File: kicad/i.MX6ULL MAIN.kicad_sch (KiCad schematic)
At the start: 3 parts

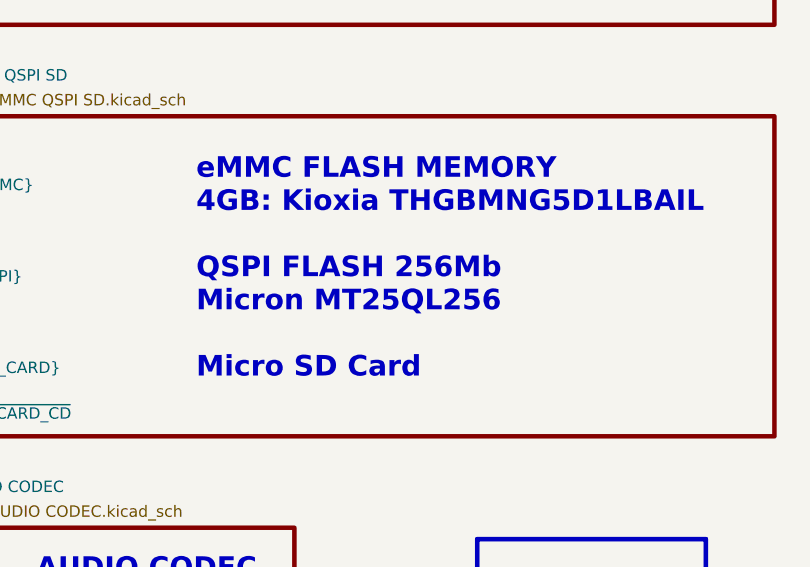
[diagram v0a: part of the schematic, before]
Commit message: Change schematic and PCB
  changed component U11 from 8MBit to 32 MBit
  added qr-code on bottom overlay
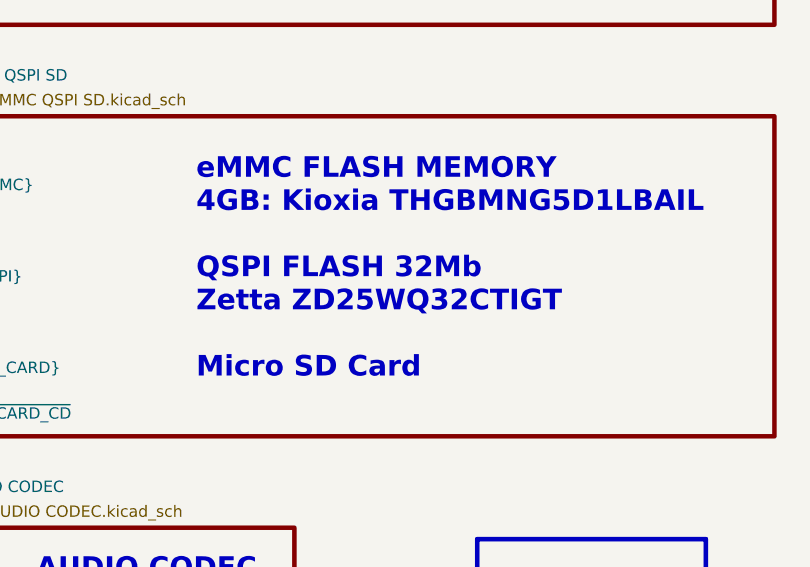
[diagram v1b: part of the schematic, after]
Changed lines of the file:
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@@
 		)
 	)
-	(text_box "eMMC FLASH MEMORY\n  4GB: Kioxia THGBMNG5D1LBAIL\n\nQSPI FLASH 256Mb\n  Micron MT25QL256\n\nMicro SD Card"
+	(text_box "eMMC FLASH MEMORY\n  4GB: Kioxia THGBMNG5D1LBAIL\n\nQSPI FLASH 32Mb\n  Zetta ZD25WQ32CTIGT\n\nMicro SD Card"
 		(exclude_from_sim no)
 		(at 317.5 93.98 0)

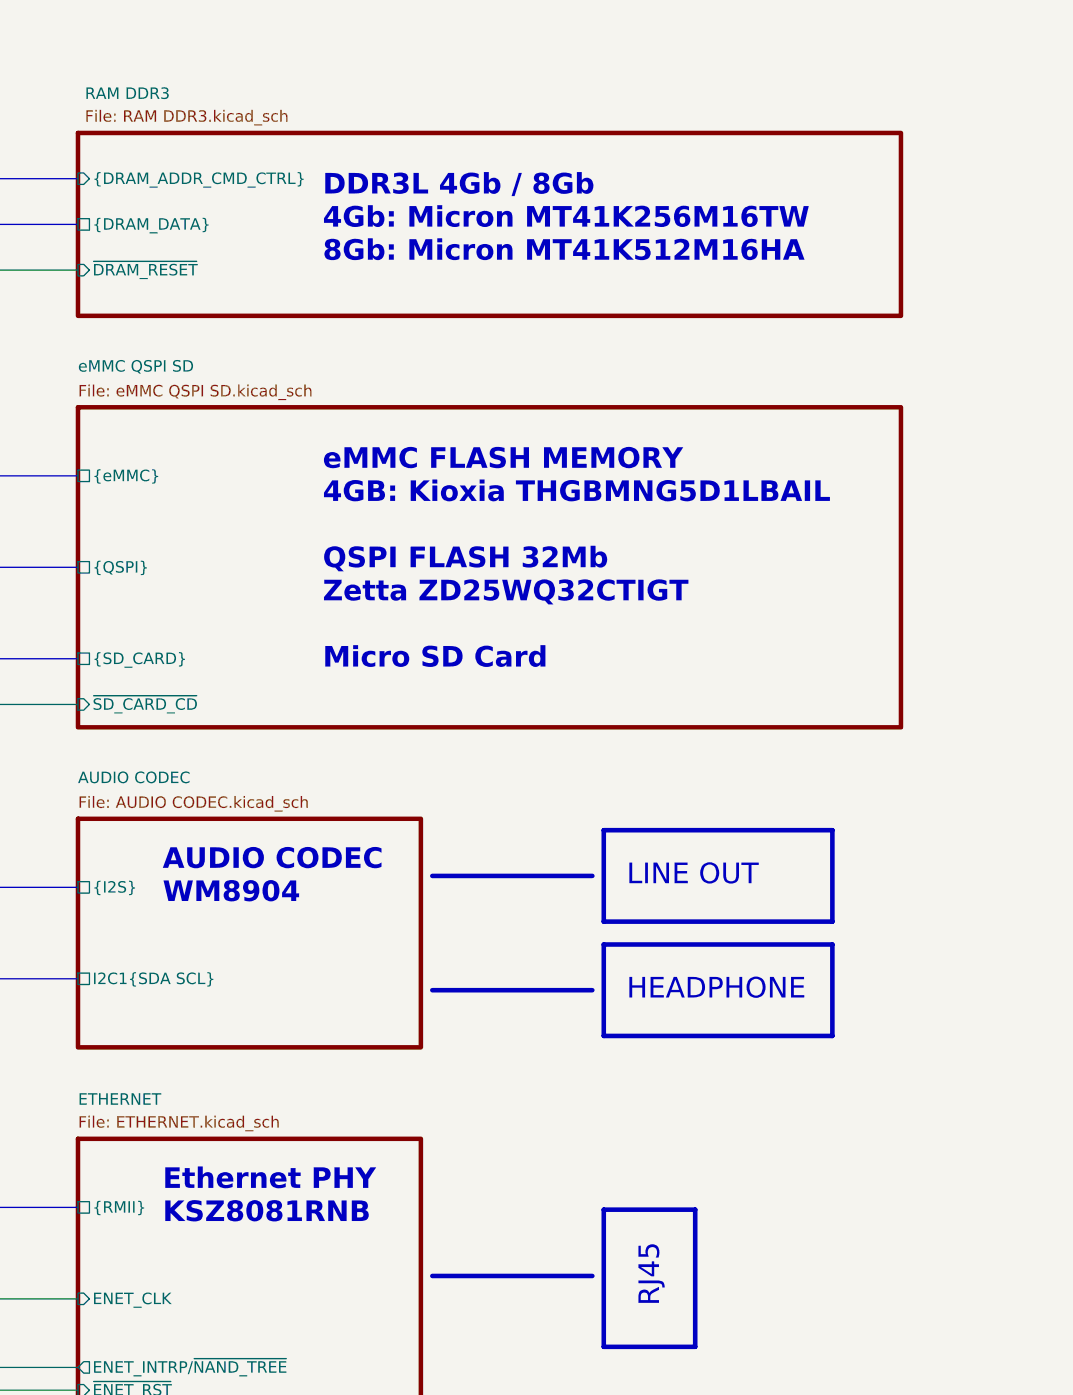
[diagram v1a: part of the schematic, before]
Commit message: Fix hardware bugs - Fix part number in bom for resistors R103, R113, R114, R118 -> 680K - Fix part number in BOM for resistors R13, R16 -> 68K - Fix part number in BOM for resistor R14 -> 4.7K - Fix part number in BOM for capacitors C100, C101, C12, C13, C130, C131, C133, C135, C140, C141, C15, C19, C57, C58, C7, C99 -> 100nF - Fix footprint for USB-A connectors - Fix power buttom pull-up resistor connection -> connect to +3.3V_STAND_BY
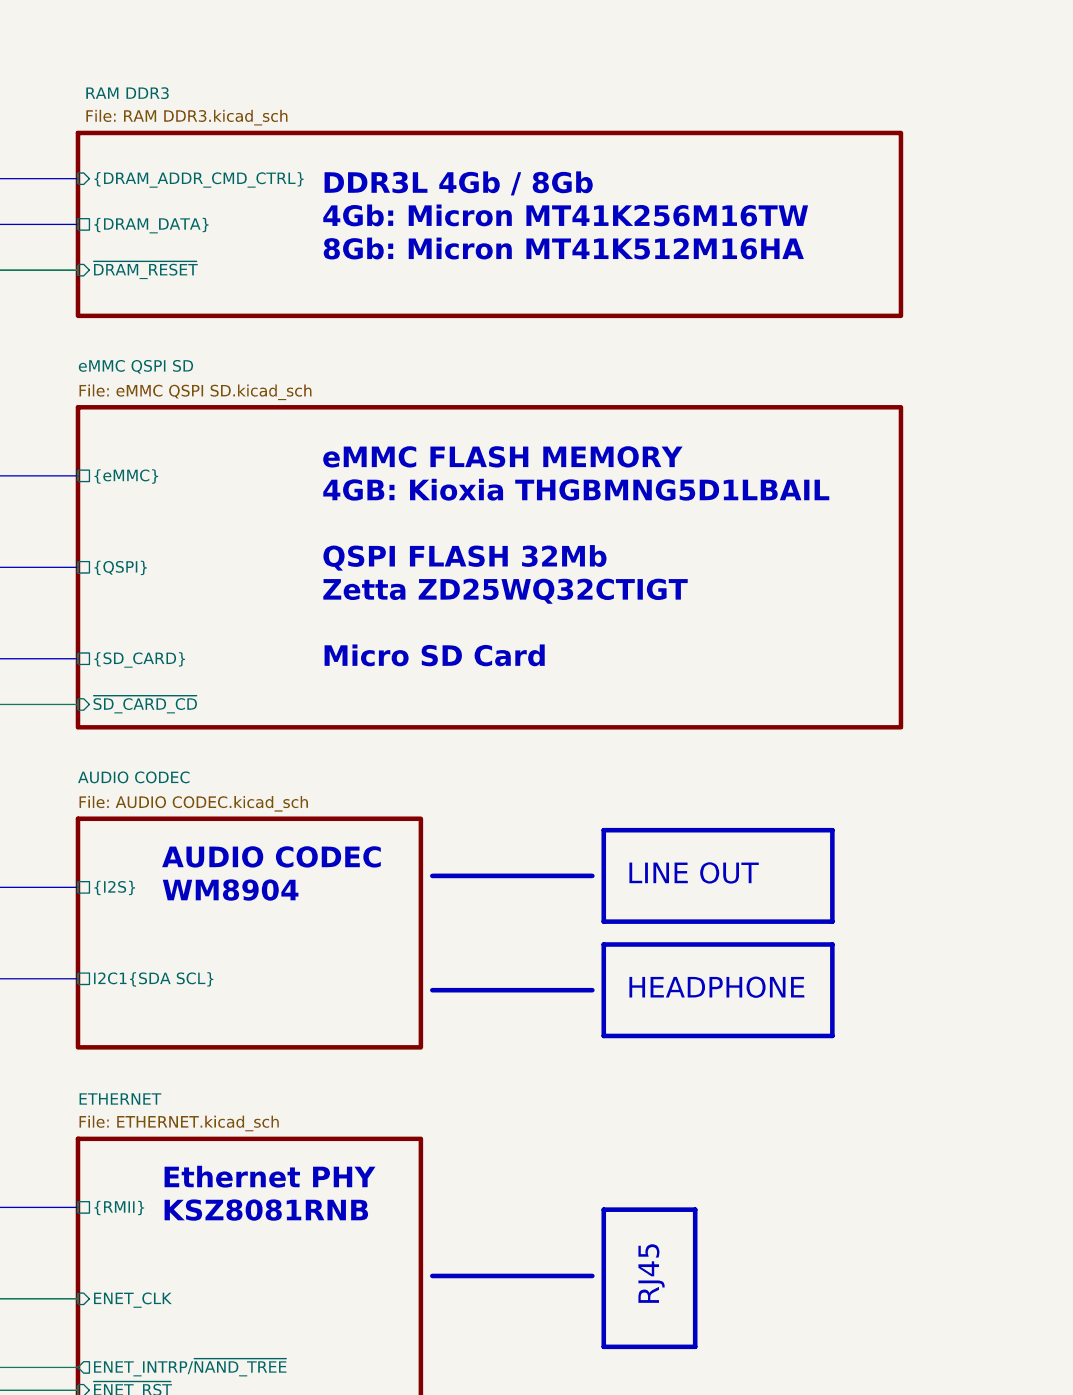
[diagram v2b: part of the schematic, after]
